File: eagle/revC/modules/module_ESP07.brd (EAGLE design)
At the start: 24.1 x 32.8 mm, 27 parts

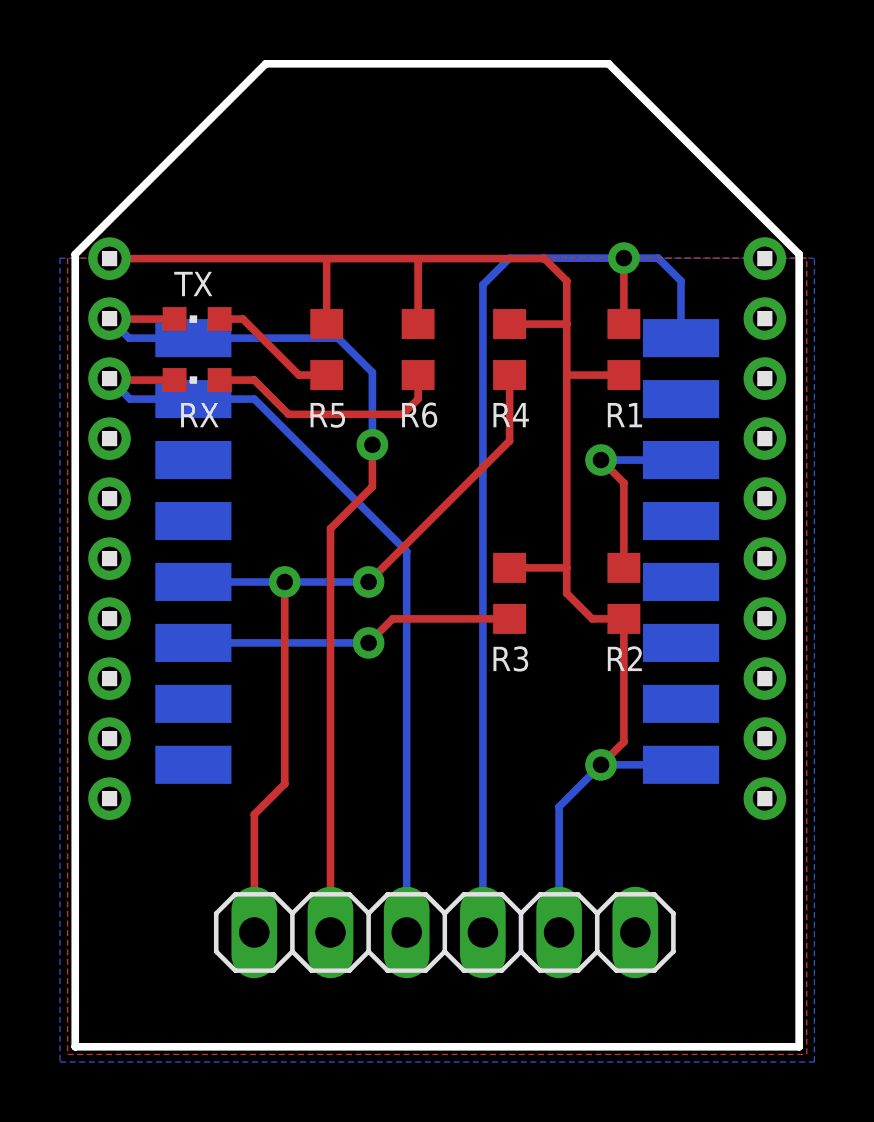
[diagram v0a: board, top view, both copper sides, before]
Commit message: Replaced modules with library parts
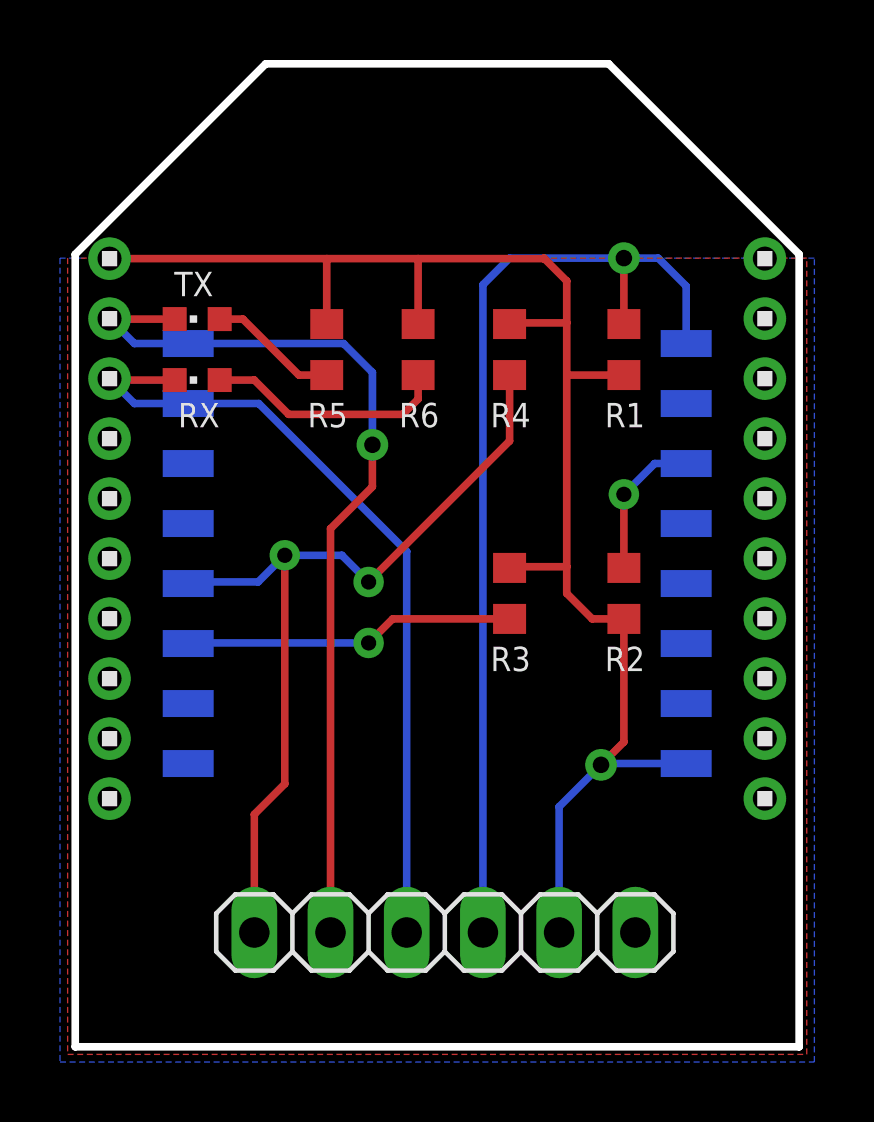
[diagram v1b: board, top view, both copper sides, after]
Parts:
- removed ADC, CH_PD, GND, GPIO0, GPIO12, GPIO13, GPIO14, GPIO15, GPIO16, GPIO2, GPIO4, GPIO5, REST, RXD, TXD, VCC: WIREPADSMD1,27-254, wirepad:SMD1,27-2,54
- added U$1: ESP-07, RadioShield:ESP07
- turned R1 to 270 degrees
- turned R2 to 270 degrees
- turned R3 to 90 degrees
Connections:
- removed net N$1: GPIO2.1, R3.2
- removed net N$2: CH_PD.1, R2.2
- new net N$6: R2.1, U$1.CH_PD
- new net N$7: R3.1, U$1.GPIO2
- net GND: now also U$1.GND, U$1.GPIO15; no longer GND.1, GPIO15.1
- net GPIO0: now also U$1.GPIO0; no longer GPIO0.1
- net RST: now also R1.1, U$1.RST; no longer R1.2, REST.1
- net UART_RX: now also U$1.RX; no longer RXD.1
- net UART_TX: now also U$1.TX; no longer TXD.1
- net VCC: now also R1.2, R2.2, R3.2, U$1.VCC; no longer R1.1, R2.1, R3.1, VCC.1
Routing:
- net N$7: track 0.00 -> 11.1 mm, vias 0 -> 1
- net N$1: track 10.9 -> 0.00 mm, vias 1 -> 0
- net N$2: track 6.58 -> 0.00 mm, vias 1 -> 0
- net N$6: track 0.00 -> 4.95 mm, vias 0 -> 1
- net GPIO0: track 26.8 -> 28.6 mm

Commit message: Fixed module name layers
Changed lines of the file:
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@@
 <wire x1="24.257" y1="26.543" x2="24.257" y2="0.127" width="0.254" layer="20"/>
 <wire x1="24.257" y1="0.127" x2="0.127" y2="0.127" width="0.254" layer="20"/>
-<text x="17.78" y="1.397" size="0.8128" layer="51" font="vector" ratio="12" rot="SR0">GND</text>
-<text x="15.367" y="1.397" size="0.8128" layer="51" font="vector" ratio="12" rot="SR0">VCC</text>
-<text x="12.827" y="1.397" size="0.8128" layer="51" font="vector" ratio="12" rot="SR0">RST</text>
-<text x="10.16" y="1.397" size="0.8128" layer="51" font="vector" ratio="12" rot="SR0">RXD</text>
-<text x="7.747" y="1.397" size="0.8128" layer="51" font="vector" ratio="12" rot="SR0">TXD</text>
-<text x="3.937" y="1.397" size="0.8128" layer="51" font="vector" ratio="12" rot="SR0">GPIO0</text>
-<text x="19.812" y="1.397" size="0.8128" layer="52" font="vector" ratio="12" rot="SMR0">GND</text>
-<text x="17.145" y="1.397" size="0.8128" layer="52" font="vector" ratio="12" rot="SMR0">VCC</text>
-<text x="14.605" y="1.397" size="0.8128" layer="52" font="vector" ratio="12" rot="SMR0">RST</text>
-<text x="12.192" y="1.397" size="0.8128" layer="52" font="vector" ratio="12" rot="SMR0">RXD</text>
-<text x="9.525" y="1.397" size="0.8128" layer="52" font="vector" ratio="12" rot="SMR0">TXD</text>
-<text x="7.112" y="1.397" size="0.8128" layer="52" font="vector" ratio="12" rot="SMR0">GPIO0</text>
-<text x="12.192" y="30.48" size="1.778" layer="51" ratio="15" rot="SR0" align="center">ESP-07</text>
+<text x="17.78" y="1.397" size="0.8128" layer="25" font="vector" ratio="12" rot="SR0">GND</text>
+<text x="15.367" y="1.397" size="0.8128" layer="25" font="vector" ratio="12" rot="SR0">VCC</text>
+<text x="12.827" y="1.397" size="0.8128" layer="25" font="vector" ratio="12" rot="SR0">RST</text>
+<text x="10.16" y="1.397" size="0.8128" layer="25" font="vector" ratio="12" rot="SR0">RXD</text>
+<text x="7.747" y="1.397" size="0.8128" layer="25" font="vector" ratio="12" rot="SR0">TXD</text>
+<text x="3.937" y="1.397" size="0.8128" layer="25" font="vector" ratio="12" rot="SR0">GPIO0</text>
+<text x="19.812" y="1.397" size="0.8128" layer="26" font="vector" ratio="12" rot="SMR0">GND</text>
+<text x="17.145" y="1.397" size="0.8128" layer="26" font="vector" ratio="12" rot="SMR0">VCC</text>
+<text x="14.605" y="1.397" size="0.8128" layer="26" font="vector" ratio="12" rot="SMR0">RST</text>
+<text x="12.192" y="1.397" size="0.8128" layer="26" font="vector" ratio="12" rot="SMR0">RXD</text>
+<text x="9.525" y="1.397" size="0.8128" layer="26" font="vector" ratio="12" rot="SMR0">TXD</text>
+<text x="7.112" y="1.397" size="0.8128" layer="26" font="vector" ratio="12" rot="SMR0">GPIO0</text>
+<text x="12.192" y="30.48" size="1.778" layer="25" ratio="15" rot="SR0" align="center">ESP-07</text>
 <text x="17.78" y="21.59" size="0.8128" layer="125" font="vector" ratio="12" rot="SR0" align="top-left">R1</text>
 <text x="17.78" y="13.462" size="0.8128" layer="125" font="vector" ratio="12" rot="SR0" align="top-left">R2</text>
